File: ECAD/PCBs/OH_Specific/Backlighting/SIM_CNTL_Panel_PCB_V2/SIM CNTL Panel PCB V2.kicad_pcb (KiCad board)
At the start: 2 copper layers, 133.9 x 76.2 mm, 116 parts, among them J1 Conn_01x04_Female, J2 Conn_01x04_Female

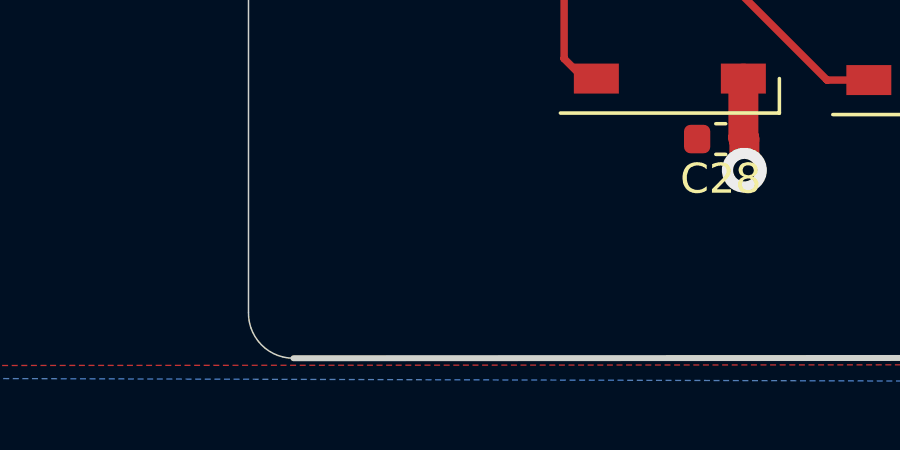
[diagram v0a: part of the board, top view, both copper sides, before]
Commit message: Latest backlighting changes
Update to multiple PCBs, mainly changing from micro-fit to mini-fit connectors.
Also changing from individual power rails to filled copper planes where possible.
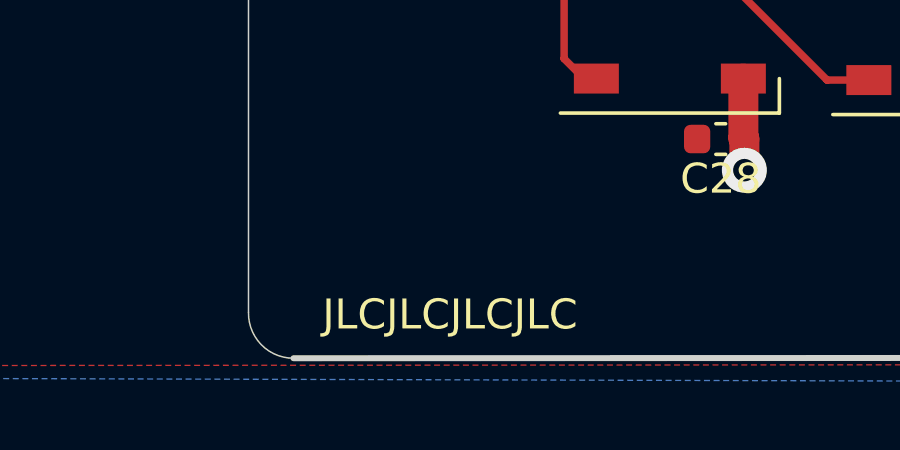
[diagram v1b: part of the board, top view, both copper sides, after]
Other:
- board text added: "JLCJLCJLCJLC"

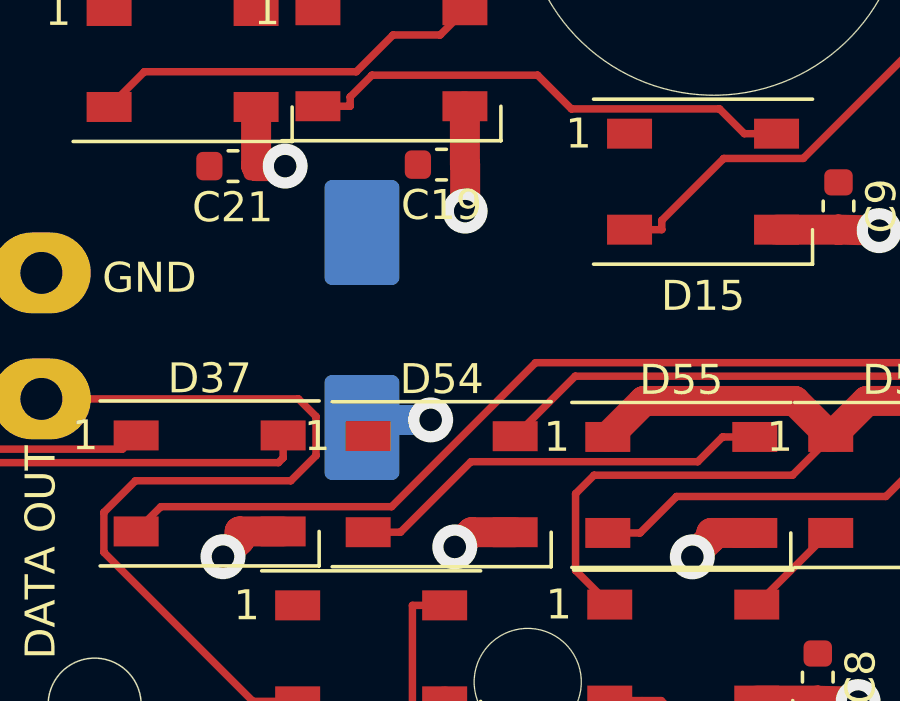
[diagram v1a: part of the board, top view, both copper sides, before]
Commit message: Right Console Backlighting changes
Changed - all right console PCBs to SW2021.
Changed - Appearance continuity set (low gloss black plastic)
Changed - SNSR panel from solid fill to thermal reliefs
Changed - SNSR panel from version 2.0 to 2.1
Changed - SIM CNTL panel from solid fill to thermal reliefs
Changed - SIM CNTL panel from version 2.0 to 2.1
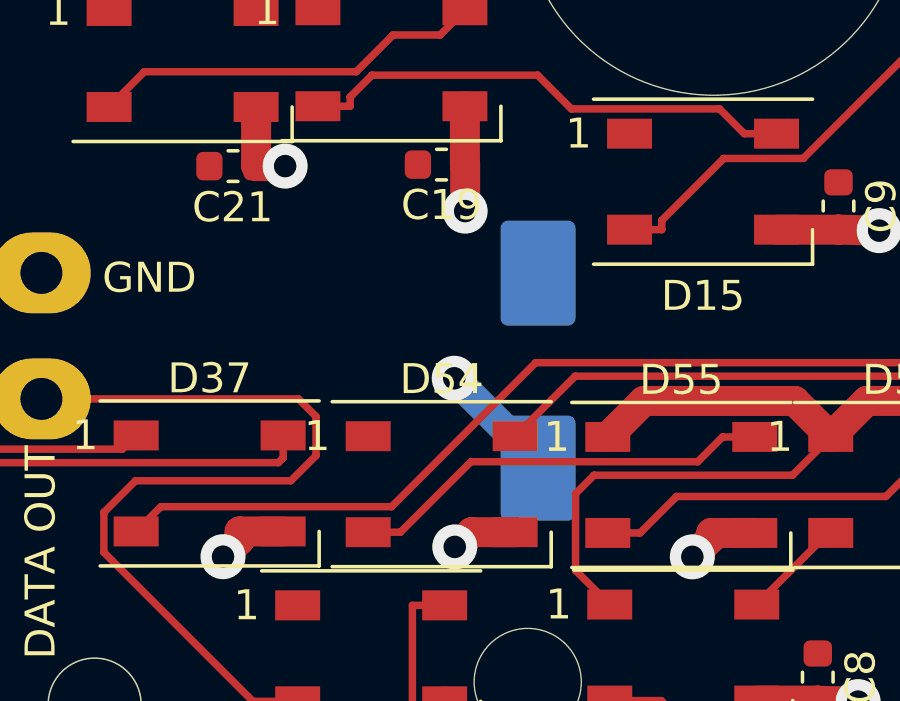
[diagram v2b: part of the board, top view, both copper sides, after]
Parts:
- moved C1 6.02 mm to (144.8, 86.9)
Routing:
- net /LED+5V: track 49.6 -> 51.4 mm
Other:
- board text added: "Version 2.1"
- board text removed: "Version 2.0"

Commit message: Revert "Merge branch 'v1.0.0-beta1' of https://github.com/jrsteensen/OpenHornet into v1.0.0-beta1"
This reverts commit f8502f84928905b30aa28383b975063036e29d04, reversing
changes made to fe5566dba69bf01016bd0ea34eb23f05549df76b.
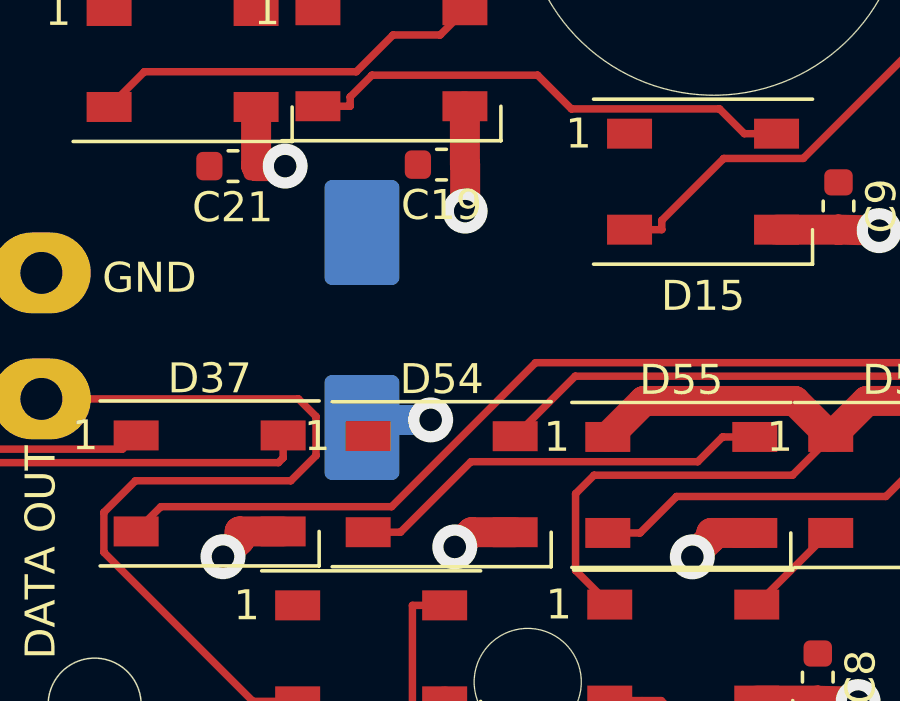
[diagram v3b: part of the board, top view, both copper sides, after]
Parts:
- moved C1 6.02 mm to (138.9, 85.5)
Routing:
- net /LED+5V: track 51.4 -> 49.6 mm
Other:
- board text added: "Version 2.0"
- board text removed: "Version 2.1"
